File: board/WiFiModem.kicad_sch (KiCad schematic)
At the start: 34 parts, among them J1 DB9_Female, J2 DB25_Male, J3 Barrel_Jack_Switch, J4 PRG, SW1 SW_Push, SW2 SW_Push, U1 ESP-12E, U2 LM7805_TO220, U3 MAX232, U4 LT1117-3.3

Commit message: swap RTS and CTS
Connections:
- net at U1.7 (GPIO13): now also R1.2, R2.1; no longer U3.10 (T2IN)
- new net: JP7.3 (B), U3.10 (T2IN)

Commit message: Added flow control enable GPIO
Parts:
- added JP8: RTSCTS, Connector_PinHeader_2.54mm:PinHeader_1x02_P2.54mm_Vertical, symbol Jumper:Jumper_2_Open
- added R9: 10k, Resistor_THT:R_Axial_DIN0207_L6.3mm_D2.5mm_P7.62mm_Horizontal, symbol Device:R
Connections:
- net +3V3: now also R9.2
- net GND: now also JP8.2 (B)
- net at U1.4 (GPIO16): now also JP8.1 (A), R9.1
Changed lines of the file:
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@@
   (junction (at 275.59 73.66) (diameter 0) (color 0 0 0 0)
   )
+  (junction (at 245.11 105.41) (diameter 0) (color 0 0 0 0)
+  )
   (junction (at 121.92 30.48) (diameter 0) (color 0 0 0 0)
   )
@@
     (stroke (width 0) (type default) (color 0 0 0 0))
   )
+  (wire (pts (xy 267.97 118.11) (xy 267.97 121.92))
+    (stroke (width 0) (type default) (color 0 0 0 0))
+  )
   (wire (pts (xy 266.7 93.98) (xy 266.7 88.9))
     (stroke (width 0) (type default) (color 0 0 0 0))
@@
     (stroke (width 0) (type default) (color 0 0 0 0))
   )
+  (wire (pts (xy 245.11 105.41) (xy 267.97 105.41))
+    (stroke (width 0) (type default) (color 0 0 0 0))
+  )
   (wire (pts (xy 121.92 85.09) (xy 121.92 86.36))
     (stroke (width 0) (type default) (color 0 0 0 0))
@@
     (stroke (width 0) (type default) (color 0 0 0 0))
   )
+  (wire (pts (xy 245.11 99.06) (xy 243.84 99.06))
+    (stroke (width 0) (type default) (color 0 0 0 0))
+  )
   (wire (pts (xy 90.17 71.12) (xy 95.25 71.12))
     (stroke (width 0) (type default) (color 0 0 0 0))
@@
     (stroke (width 0) (type default) (color 0 0 0 0))
   )
+  (wire (pts (xy 245.11 99.06) (xy 245.11 105.41))
+    (stroke (width 0) (type default) (color 0 0 0 0))
+  )
   (wire (pts (xy 243.84 73.66) (xy 275.59 73.66))
     (stroke (width 0) (type default) (color 0 0 0 0))
@@
     (stroke (width 0) (type default) (color 0 0 0 0))
   )
+  (wire (pts (xy 238.76 113.03) (xy 245.11 113.03))
+    (stroke (width 0) (type default) (color 0 0 0 0))
+  )
   (wire (pts (xy 180.34 120.65) (xy 180.34 124.46))
     (stroke (width 0) (type default) (color 0 0 0 0))
@@
     (stroke (width 0) (type default) (color 0 0 0 0))
   )
+  (wire (pts (xy 267.97 107.95) (xy 267.97 105.41))
+    (stroke (width 0) (type default) (color 0 0 0 0))
+  )
   (wire (pts (xy 36.83 63.5) (xy 40.64 63.5))
     (stroke (width 0) (type default) (color 0 0 0 0))
@@
   )
   (wire (pts (xy 204.47 62.23) (xy 204.47 52.07))
+    (stroke (width 0) (type default) (color 0 0 0 0))
+  )
+  (wire (pts (xy 238.76 111.76) (xy 238.76 113.03))
     (stroke (width 0) (type default) (color 0 0 0 0))
   )
@@
     (pin "2")
   )
+  (symbol (lib_id "Jumper:Jumper_2_Open") (at 267.97 113.03 270) (unit 1)
+    (in_bom yes) (on_board yes) (fields_autoplaced)
+    (property "Reference" "JP8" (id 0) (at 270.51 111.7599 90)
+      (effects (font (size 1.27 1.27)) (justify left))
+    )
+    (property "Value" "RTSCTS" (id 1) (at 270.51 114.2999 90)
+      (effects (font (size 1.27 1.27)) (justify left))
+    )
+    (property "Footprint" "Connector_PinHeader_2.54mm:PinHeader_1x02_P2.54mm_Vertical" (id 2) (at 267.97 113.03 0)
+      (effects (font (size 1.27 1.27)) hide)
+    )
+    (property "Datasheet" "~" (id 3) (at 267.97 113.03 0)
+      (effects (font (size 1.27 1.27)) hide)
+    )
+    (pin "1")
+    (pin "2")
+  )
   (symbol (lib_id "Connector_Generic:Conn_01x03") (at 264.16 99.06 270) (unit 1)
     (in_bom yes) (on_board yes)
@@
     (pin "9")
   )
+  (symbol (lib_id "Device:R") (at 245.11 109.22 0) (unit 1)
+    (in_bom yes) (on_board yes)
+    (property "Reference" "R9" (id 0) (at 247.65 107.9499 0)
+      (effects (font (size 1.27 1.27)) (justify left))
+    )
+    (property "Value" "10k" (id 1) (at 245.11 110.49 90)
+      (effects (font (size 1.27 1.27)) (justify left))
+    )
+    (property "Footprint" "Resistor_THT:R_Axial_DIN0207_L6.3mm_D2.5mm_P7.62mm_Horizontal" (id 2) (at 243.332 109.22 90)
+      (effects (font (size 1.27 1.27)) hide)
+    )
+    (property "Datasheet" "~" (id 3) (at 245.11 109.22 0)
+      (effects (font (size 1.27 1.27)) hide)
+    )
+    (pin "1")
+    (pin "2")
+  )
   (symbol (lib_id "power:+3.3V") (at 228.6 49.53 0) (unit 1)
     (in_bom yes) (on_board yes) (fields_autoplaced)
@@
     (pin "2")
   )
+  (symbol (lib_id "power:GND") (at 267.97 121.92 0) (unit 1)
+    (in_bom yes) (on_board yes) (fields_autoplaced)
+    (property "Reference" "#PWR0127" (id 0) (at 267.97 128.27 0)
+      (effects (font (size 1.27 1.27)) hide)
+    )
+    (property "Value" "GND" (id 1) (at 267.97 127 0))
+    (property "Footprint" "" (id 2) (at 267.97 121.92 0)
+      (effects (font (size 1.27 1.27)) hide)
+    )
+    (property "Datasheet" "" (id 3) (at 267.97 121.92 0)
+      (effects (font (size 1.27 1.27)) hide)
+    )
+    (pin "1")
+  )
   (symbol (lib_id "Regulator_Linear:LT1117-3.3") (at 182.88 30.48 0) (unit 1)
     (in_bom yes) (on_board yes) (fields_autoplaced)
@@
     (pin "2")
   )
+  (symbol (lib_id "power:+3.3V") (at 238.76 111.76 0) (unit 1)
+    (in_bom yes) (on_board yes) (fields_autoplaced)
+    (property "Reference" "#PWR0126" (id 0) (at 238.76 115.57 0)
+      (effects (font (size 1.27 1.27)) hide)
+    )
+    (property "Value" "+3.3V" (id 1) (at 238.76 106.68 0))
+    (property "Footprint" "" (id 2) (at 238.76 111.76 0)
+      (effects (font (size 1.27 1.27)) hide)
+    )
+    (property "Datasheet" "" (id 3) (at 238.76 111.76 0)
+      (effects (font (size 1.27 1.27)) hide)
+    )
+    (pin "1")
+  )
   (symbol (lib_id "Regulator_Linear:LM7805_TO220") (at 132.08 30.48 0) (unit 1)
     (in_bom yes) (on_board yes) (fields_autoplaced)
@@
       (reference "#PWR0125") (unit 1) (value "GND") (footprint "")
     )
+    (path "/f932d73e-00aa-43b0-be31-777f62560224"
+      (reference "#PWR0126") (unit 1) (value "+3.3V") (footprint "")
+    )
+    (path "/85c22c96-8aa9-4729-b651-96556c3913e3"
+      (reference "#PWR0127") (unit 1) (value "GND") (footprint "")
+    )
     (path "/1ac58922-666e-4555-b3c0-e472821a0ed9"
       (reference "C1") (unit 1) (value "10 uF") (footprint "Capacitor_THT:CP_Radial_D5.0mm_P2.00mm")
@@
       (reference "JP7") (unit 1) (value "PROG") (footprint "Connector_PinHeader_2.54mm:PinHeader_1x03_P2.54mm_Vertical")
     )
+    (path "/2cfe946b-ef42-4712-aba1-8371f5f81b04"
+      (reference "JP8") (unit 1) (value "RTSCTS") (footprint "Connector_PinHeader_2.54mm:PinHeader_1x02_P2.54mm_Vertical")
+    )
     (path "/ed4f2a97-7862-4c00-9260-110c4aa8ea06"
       (reference "R1") (unit 1) (value "470R") (footprint "Resistor_THT:R_Axial_DIN0207_L6.3mm_D2.5mm_P7.62mm_Horizontal")
@@
       (reference "R8") (unit 1) (value "10k") (footprint "Resistor_THT:R_Axial_DIN0207_L6.3mm_D2.5mm_P7.62mm_Horizontal")
     )
+    (path "/6792a032-9256-487f-aa0b-8c689e242f4e"
+      (reference "R9") (unit 1) (value "10k") (footprint "Resistor_THT:R_Axial_DIN0207_L6.3mm_D2.5mm_P7.62mm_Horizontal")
+    )
     (path "/bedc2388-6214-4257-bb4d-a226144e1b11"

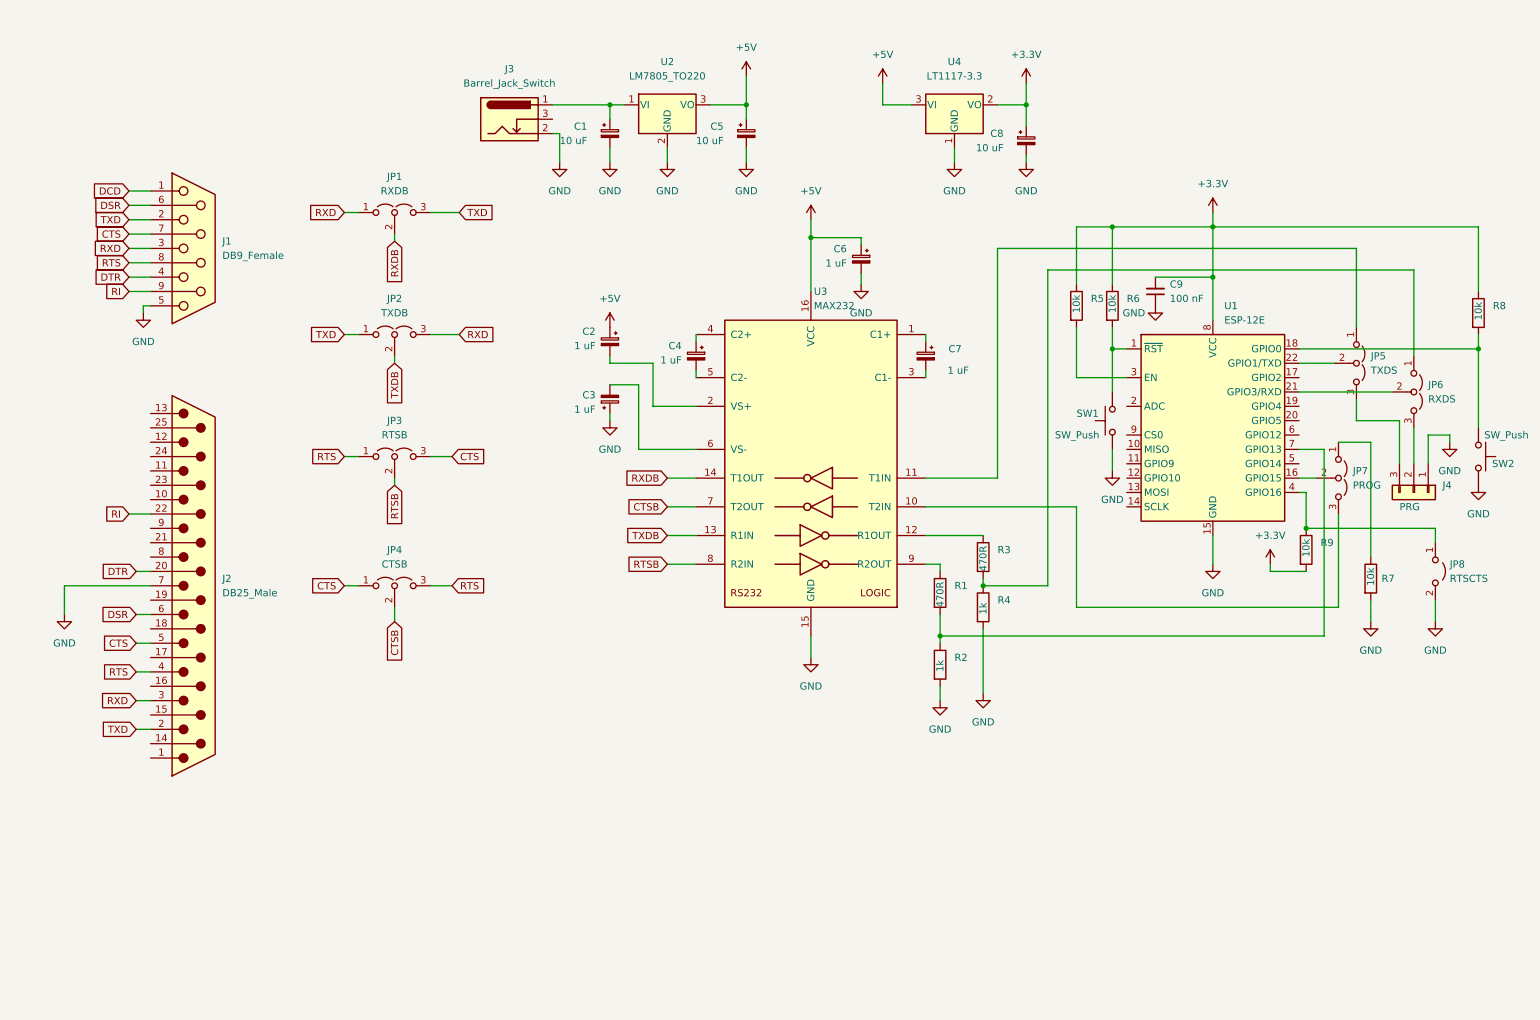
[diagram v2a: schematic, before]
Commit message: Added all of the other control signals
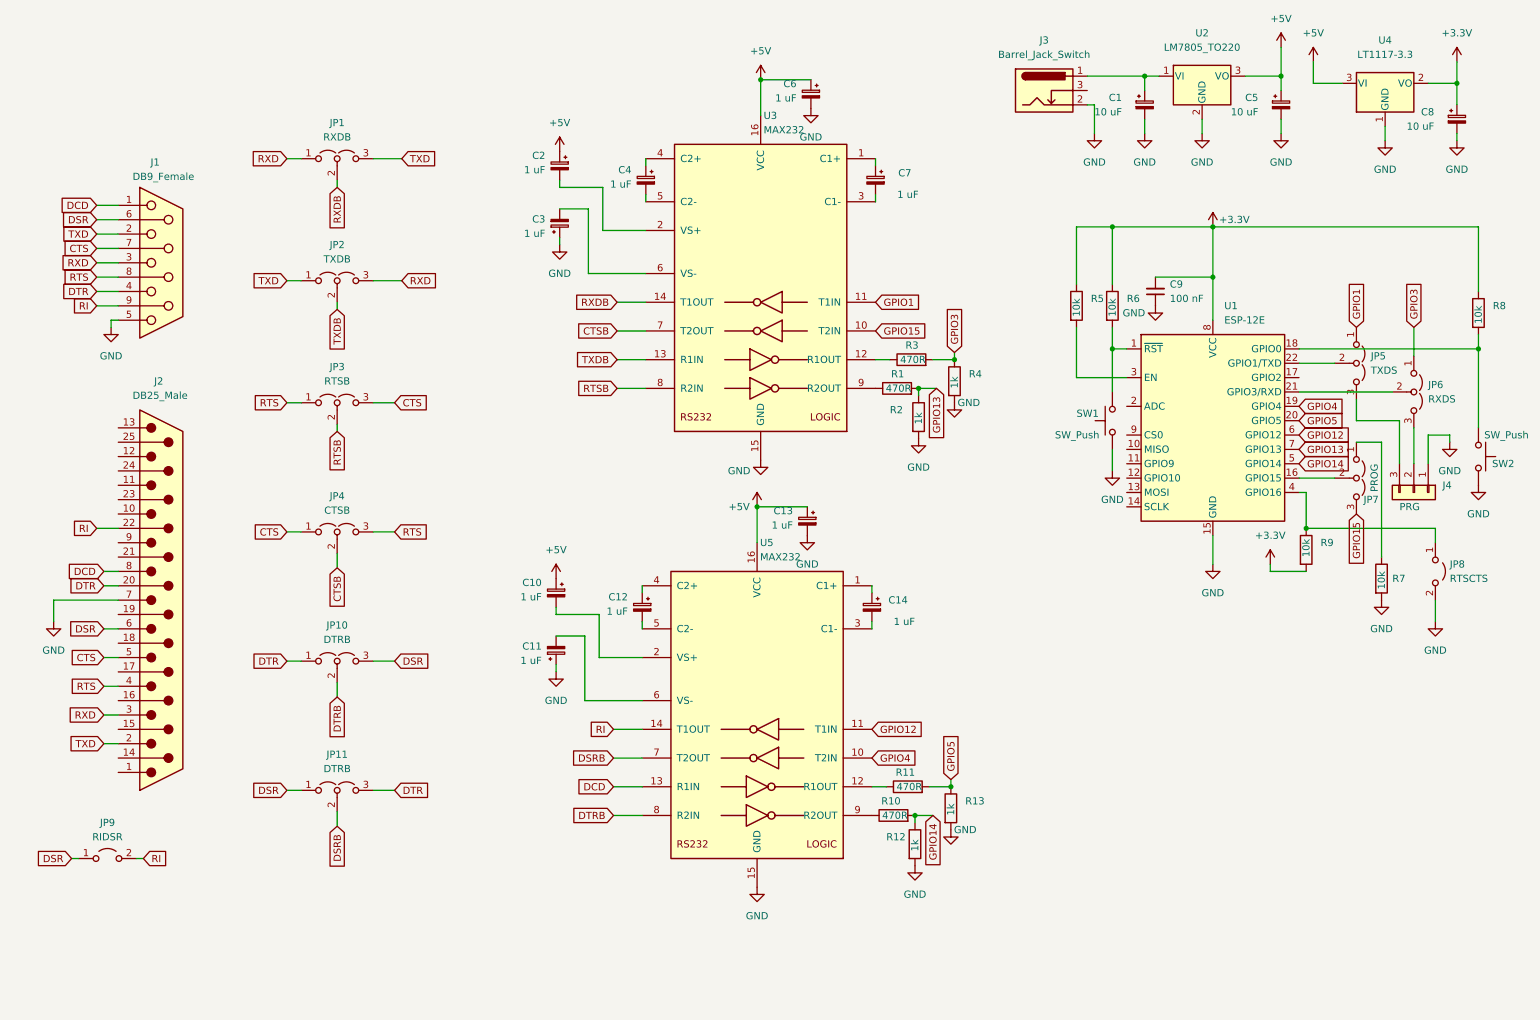
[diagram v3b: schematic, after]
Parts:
- added C10, C11, C12, C13, C14: 1 uF, Capacitor_THT:CP_Radial_D5.0mm_P2.00mm, symbol Device:C_Polarized_Small
- added JP10, JP11: DTRB, Connector_PinHeader_2.54mm:PinHeader_1x03_P2.54mm_Vertical, symbol Jumper:Jumper_3_Open
- added JP9: RIDSR, Connector_PinHeader_2.54mm:PinHeader_1x02_P2.54mm_Vertical, symbol Jumper:Jumper_2_Open
- added R10, R11: 470R, Resistor_THT:R_Axial_DIN0207_L6.3mm_D2.5mm_P7.62mm_Horizontal, symbol Device:R
- added R12, R13: 1k, Resistor_THT:R_Axial_DIN0207_L6.3mm_D2.5mm_P7.62mm_Horizontal, symbol Device:R
- added U5: MAX232, Package_DIP:DIP-16_W7.62mm_Socket, symbol Interface_UART:MAX232
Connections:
- net +5V: now also C10.1, C13.1, U5.16 (VCC)
- net DCD: now also J2.8, U5.13 (R1IN)
- net DSR: now also JP10.3 (B), JP11.1 (A), JP9.1 (A)
- net DTR: now also JP10.1 (A), JP11.3 (B)
- net GND: now also C11.1, C13.2, R12.2, R13.2, U5.15 (GND)
- net RI: now also JP9.2 (B), U5.14 (T1OUT)
- net GPIO3: now reaches JP6.1 (A), R3.2, R4.1
- net GPIO4: now reaches U1.19 (GPIO4)
- net GPIO4: now also U5.10 (T2IN)
- net GPIO5: now reaches U1.20 (GPIO5)
- net GPIO5: now also R11.2, R13.1
- net GPIO14: now reaches U1.5 (GPIO14)
- net GPIO14: now also R10.2, R12.1
- net GPIO12: now reaches U1.6 (GPIO12)
- net GPIO12: now also U5.11 (T1IN)
- net GPIO13: now reaches R1.2, R2.1, U1.7 (GPIO13)
- net GPIO15: now reaches JP7.3 (B), U3.10 (T2IN)
- net GPIO1: now reaches JP5.1 (A), U3.11 (T1IN)
- new net: R11.1, U5.12 (R1OUT)
- new net: R10.1, U5.9 (R2OUT)
- new net: C11.2, U5.6 (VS-)
- new net: C12.1, U5.4 (C2+)
- new net: C12.2, U5.5 (C2-)
- new net: C14.1, U5.1 (C1+)
- new net: C14.2, U5.3 (C1-)
- new net: C10.2, U5.2 (VS+)
- new net DSRB: JP11.2 (C), U5.7 (T2OUT)
- new net DTRB: JP10.2 (C), U5.8 (R2IN)
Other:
- moved on the sheet: C1, C2, C3, C4, C5, C6, C7, C8, J1, J2, J3, JP1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

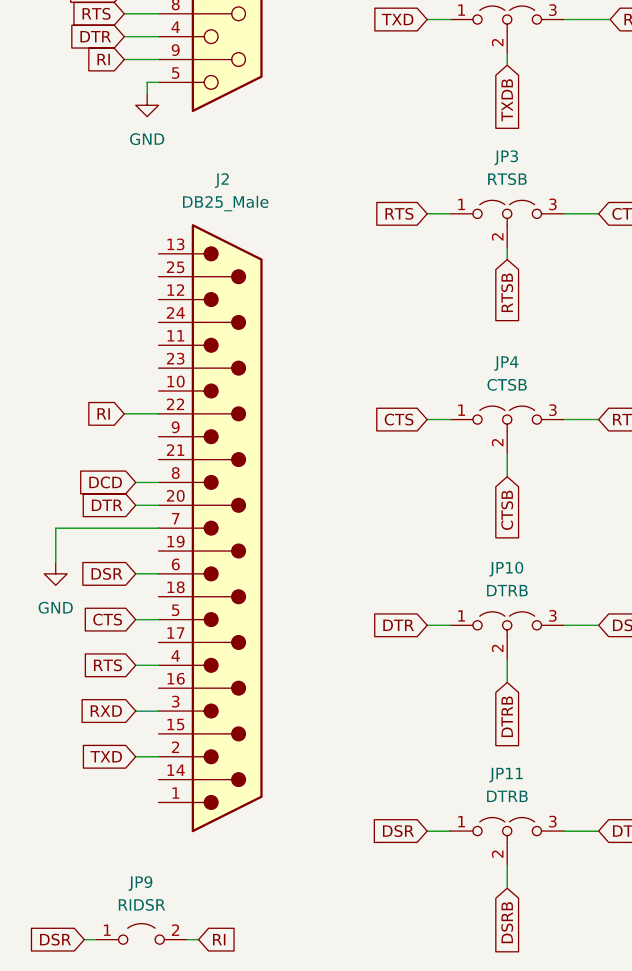
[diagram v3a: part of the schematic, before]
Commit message: Changed from DB25 male to DB25 female
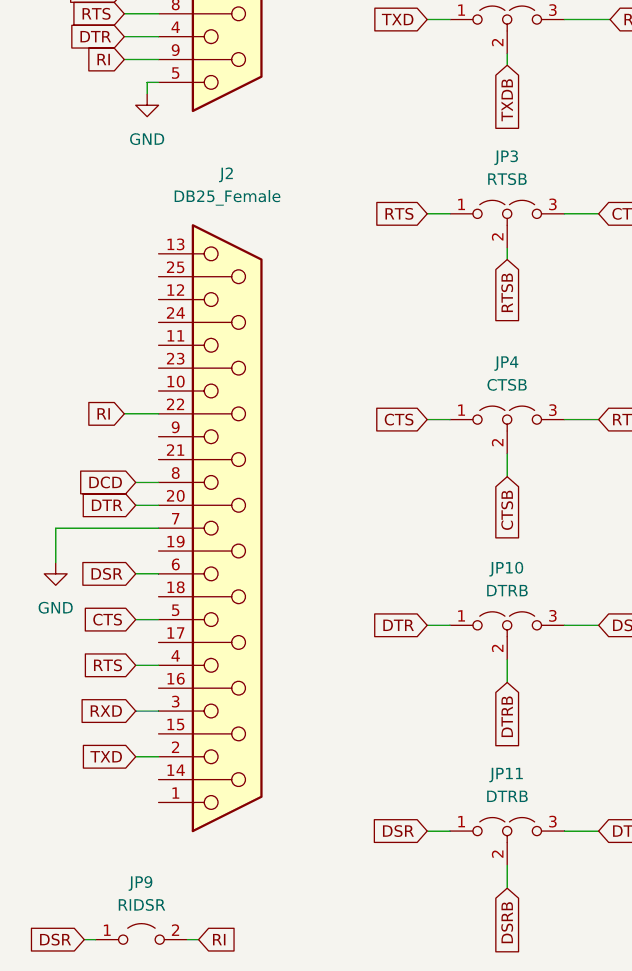
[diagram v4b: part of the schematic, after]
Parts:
- removed J2: DB25_Male, Connector_Dsub:DSUB-25_Male_Horizontal_P2.77x2.84mm_EdgePinOffset7.70mm_Housed_MountingHolesOffset9.12mm, symbol Connector:DB25_Male
- added J2: DB25_Female, Connector_Dsub:DSUB-25_Female_Horizontal_P2.77x2.84mm_EdgePinOffset7.70mm_Housed_MountingHolesOffset9.12mm, symbol Connector:DB25_Female
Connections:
- net CTS: now also J2.5
- net DCD: now also J2.8
- net DSR: now also J2.6
- net DTR: now also J2.20 (P20)
- net GND: now also J2.7
- net RI: now also J2.22 (P22)
- net RTS: now also J2.4
- net RXD: now also J2.3
- net TXD: now also J2.2
